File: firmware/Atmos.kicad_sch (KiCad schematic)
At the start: 71 parts, among them J1 AS3935 breakout, J2 BME280 breakout, J3 USB_C_Receptacle_USB2.0_16P, J4 Micro_SD_Card, J5 Solar power input, J6 Conn_Coaxial, Q1 PMOS_Substrate, Q2 PMOS_Substrate, Q3 PMOS_Substrate, SW2 SW_Push, U1 ESP32-S3-WROOM-1, U10 TPS22918DBVR, U11 MAX17048G_T10, U12 CN3791, U13 SGP40-D-R4, U2 AP2112K-3.3, U3 DS3231M, U4 PMS5003, U5 LTC4412xS6, U7 RFM95W-915S2, U8 USBLC6-2SC6, U9 TPS61023DRLR

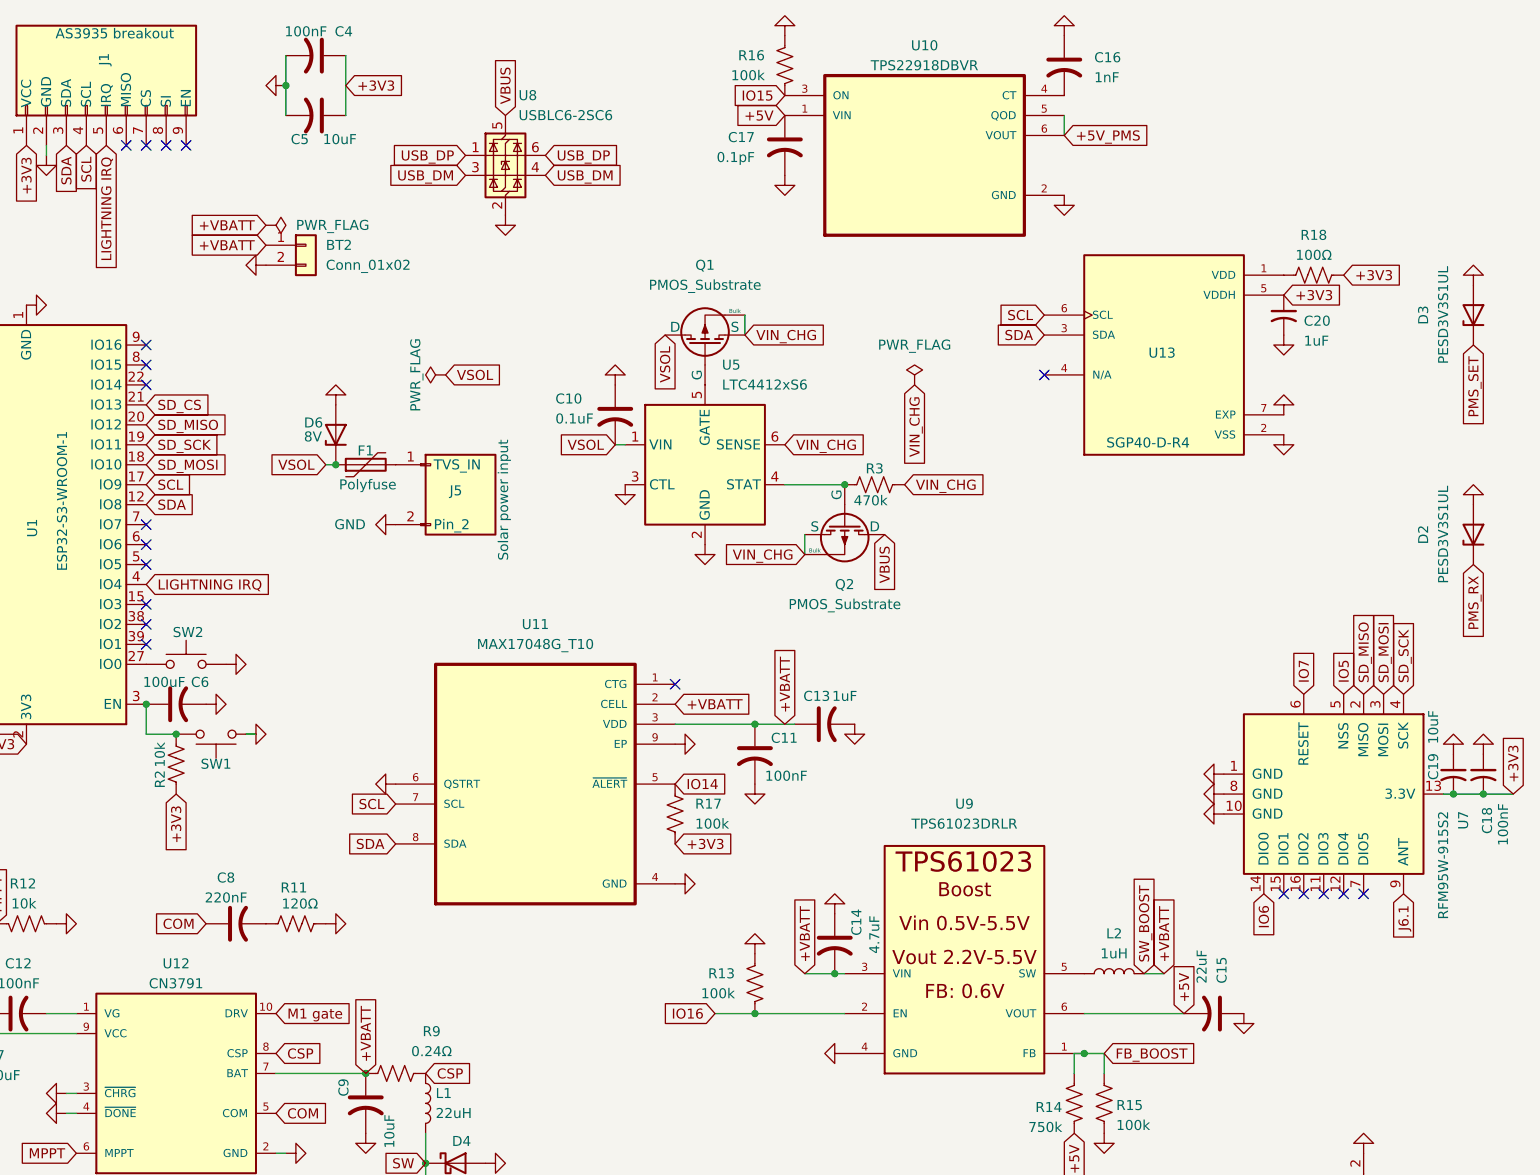
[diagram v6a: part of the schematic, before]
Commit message: Schematic fully finished -hierarchies
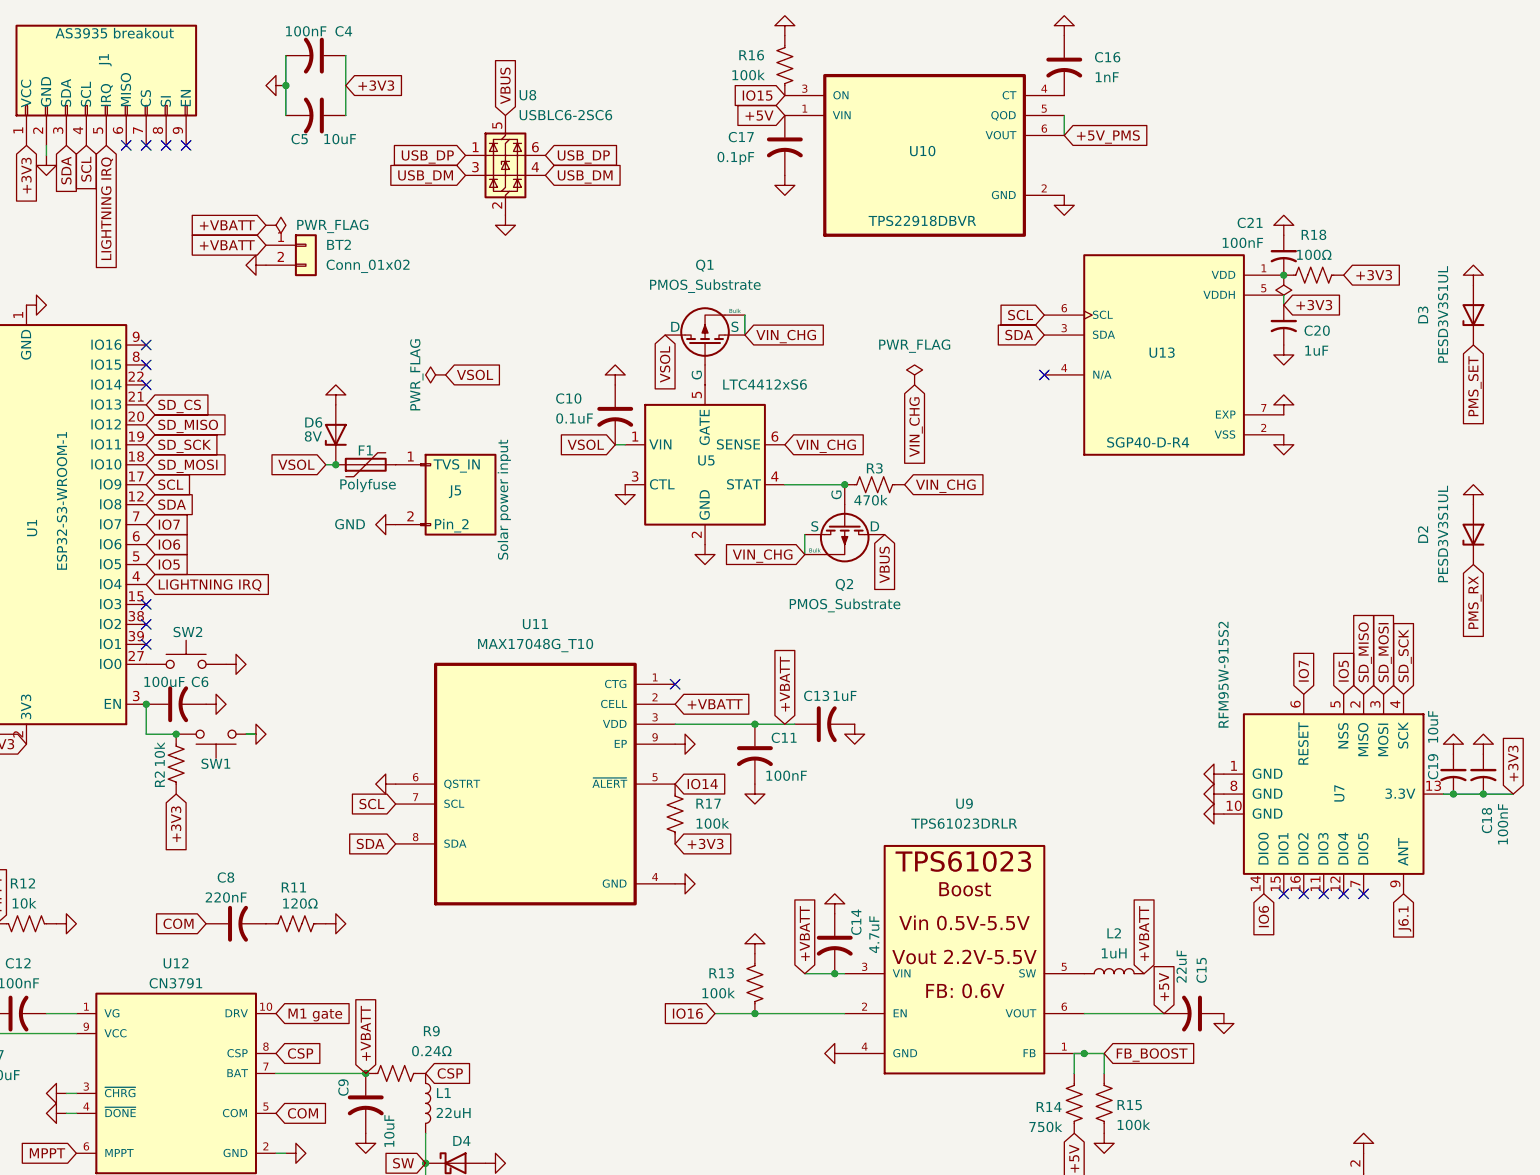
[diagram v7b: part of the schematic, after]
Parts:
- added C21: 100nF, symbol Device:C_Small_US
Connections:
- net GND: now also C21.1
- net IO5: now also U1.5 (IO5)
- net IO6: now also U1.6 (IO6)
- net IO7: now also U1.7 (IO7)
- net at R18.1, U13.1 (VDD): now also C21.2
- no-connect marks 48 -> 45
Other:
- moved on the sheet: C15, C20

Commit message: updated a few values
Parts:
- C17: value 0.1pF -> 100nF
- C6: value 100uF -> 1uF
- R3: value 470k -> 1M
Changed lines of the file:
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@@
 			)
 		)
-		(property "Value" "0.1pF"
+		(property "Value" "100nF"
 			(at 189.23 30.7339 0)
 			(effects
@@
 			)
 		)
-		(property "Value" "470k"
+		(property "Value" "1M"
 			(at 203.962 74.422 90)
 			(effects
@@
 			)
 		)
-		(property "Value" "100uF"
+		(property "Value" "1uF"
 			(at 114.046 97.536 90)
 			(effects
